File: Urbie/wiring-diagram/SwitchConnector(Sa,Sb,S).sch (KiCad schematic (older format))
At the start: 6 parts

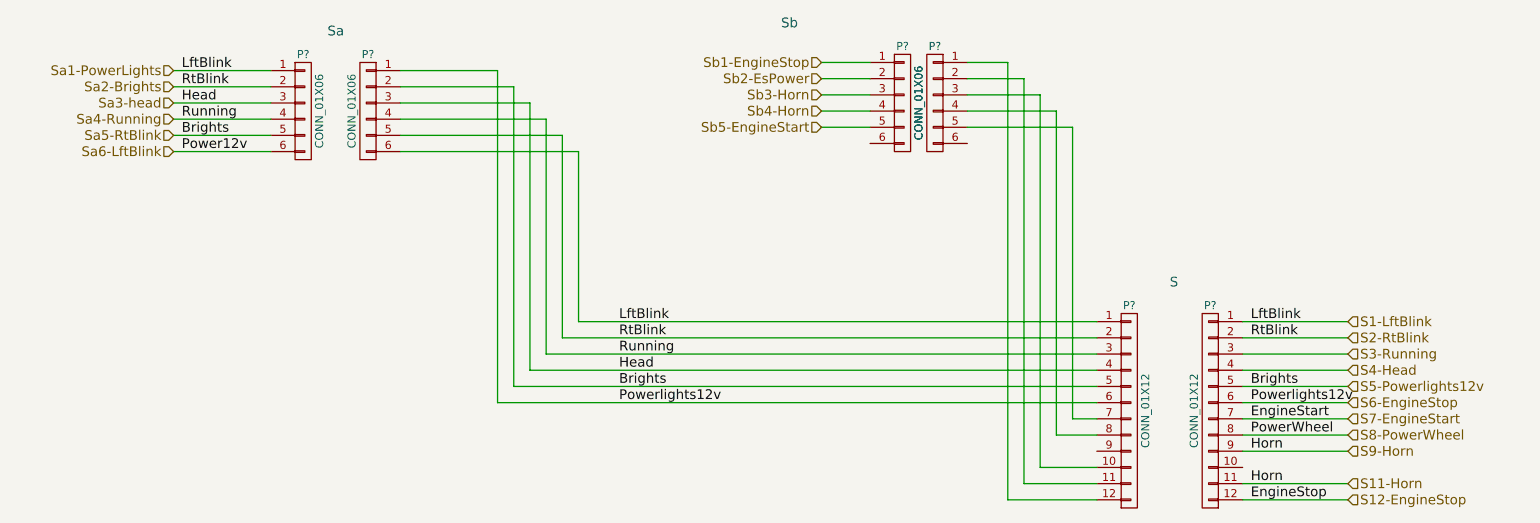
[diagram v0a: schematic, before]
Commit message: cleaning up schematics
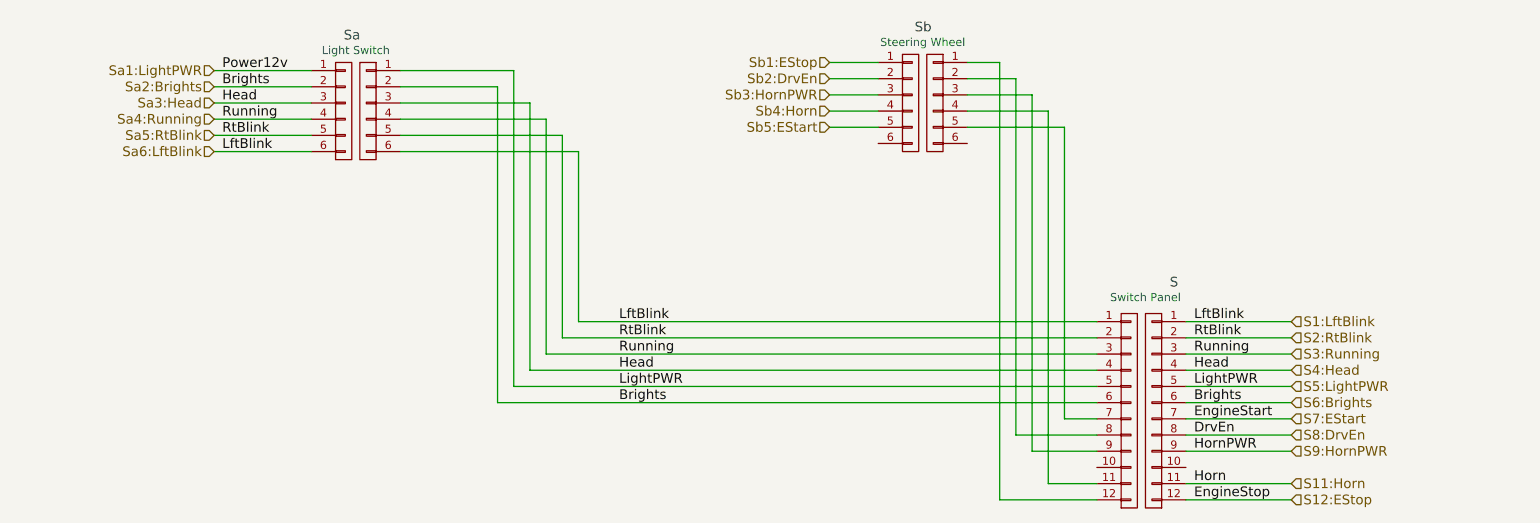
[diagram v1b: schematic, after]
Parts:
- P?: value CONN_01X06 -> Light Switch
- P?: value CONN_01X06 -> Steering Wheel
- P?: value CONN_01X12 -> Switch Panel
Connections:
- net Sa3-head is gone; now on net S4:Head: P?.3 (P3), P?.3 (P3), P?.4 (P4)
- net Sa4-Running is gone; now on net S3:Running: P?.3 (P3), P?.4 (P4), P?.4 (P4)
- net Sa6-LftBlink is gone; now on net S1:LftBlink: P?.6 (P6)
- net at P?.2 (P2): now also P?.8 (P8); no longer P?.11 (P11)
- net at P?.3 (P3): now also P?.9 (P9); no longer P?.10 (P10)
- net at P?.4 (P4): now also P?.11 (P11); no longer P?.8 (P8)
- net S1-LftBlink renamed S1:LftBlink
- net S1:LftBlink: no longer P?.1 (P1)
- net S11-Horn renamed S11:Horn
- net S11:Horn: no longer P?.9 (P9)
- net S12-EngineStop renamed S12:EStop
- net S2-RtBlink renamed S2:RtBlink
- net S2:RtBlink: now also P?.5 (P5); no longer P?.2 (P2)
- net S3-Running renamed S3:Running
- net S4-Head renamed S4:Head
- net S5-Powerlights12v renamed S5:LightPWR
- net S5:LightPWR: now also P?.1 (P1); no longer P?.2 (P2), P?.5 (P5)
- net S6-EngineStop renamed S6:Brights
- net S6:Brights: now also P?.2 (P2), P?.2 (P2); no longer P?.1 (P1)
- net S7-EngineStart renamed S7:EStart
- net S8-PowerWheel renamed S8:DrvEn
- net Sb1-EngineStop renamed Sb1:EStop
- net Sb2-EsPower renamed Sb2:DrvEn
- net Sb3-Horn renamed Sb3:HornPWR
- net Sb4-Horn renamed Sb4:Horn
- net Sb5-EngineStart renamed Sb5:EStart
- new net S9:HornPWR: P?.9 (P9)
- new net Sa1:LightPWR: P?.1 (P1)
